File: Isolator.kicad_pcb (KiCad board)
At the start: 2 copper layers, 33 x 67.3 mm, 35 parts, among them J1 Step_0_In, J2 Step_0_Out, J3 Step_1_In, J4 Step_1_Out, J5 UART_In, J6 UART_Out, U1 ISO6741, U2 ISO6741, U3 ISO6721

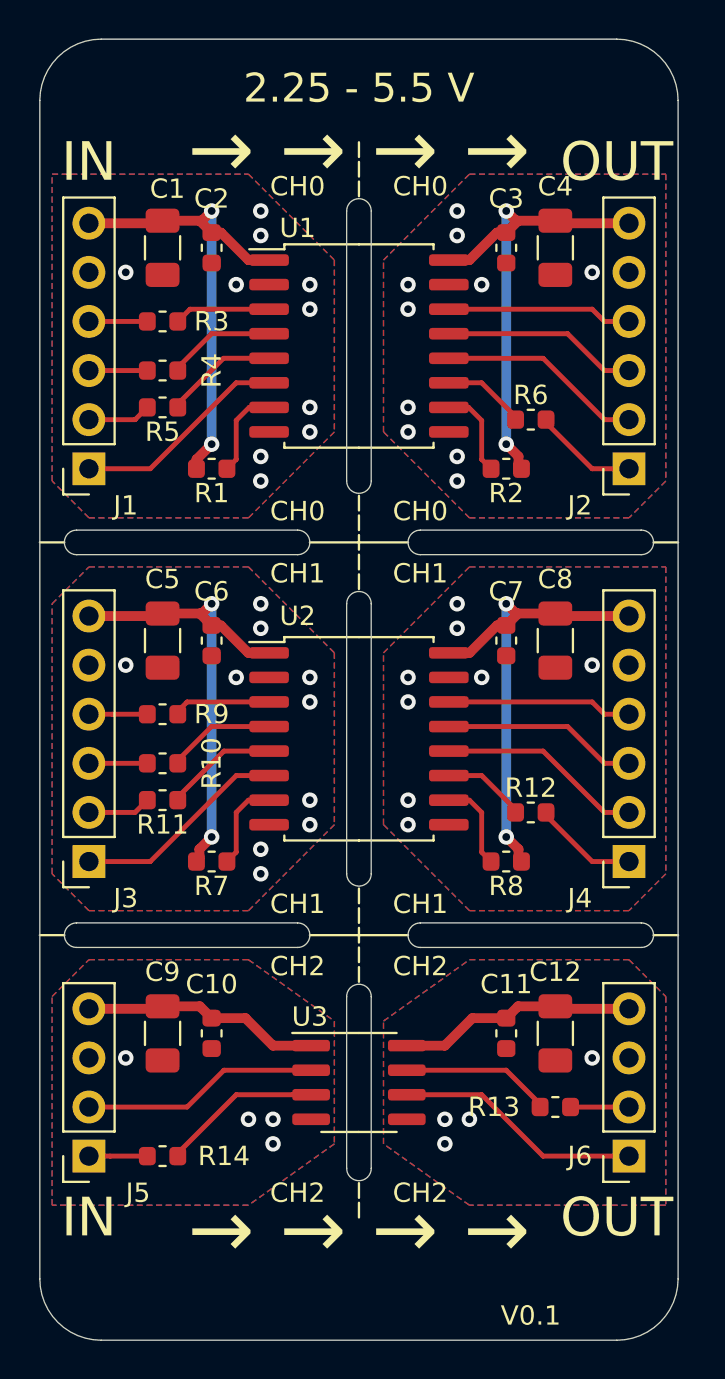
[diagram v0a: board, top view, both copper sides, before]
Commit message: Added mounting holes. (They got lost somehow)
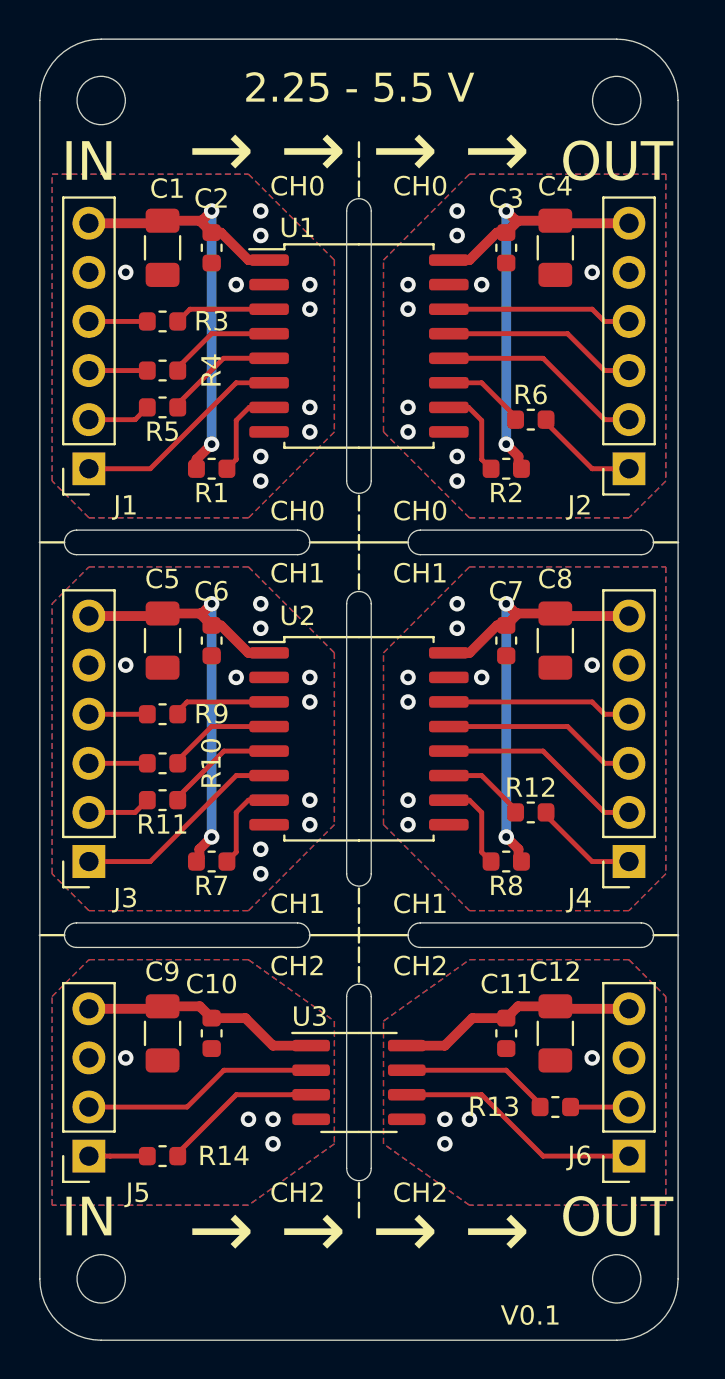
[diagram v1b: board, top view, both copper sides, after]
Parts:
- added  : , MountingHole:MountingHole_2.5mm, F.Cu at (142.9, 55.9)
- added  : , MountingHole:MountingHole_2.5mm, F.Cu at (169.5, 55.9)
- added  : , MountingHole:MountingHole_2.5mm, F.Cu at (169.5, 116.8)
- added  : , MountingHole:MountingHole_2.5mm, F.Cu at (142.9, 116.8)
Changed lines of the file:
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@@
     (tracks 213)
     (zones 0)
-    (modules 35)
+    (modules 39)
     (nets 47)
   )
@@
     (add_net "Net-(R9-Pad2)")
   )
+  (module MountingHole:MountingHole_2.5mm (layer F.Cu)
+    (at 142.875 55.88)
+    (descr "Mounting Hole 2.5mm, no annular")
+    (tags "mounting hole 2.5mm no annular")
+    (attr virtual)
+    (fp_text reference " " (at 0 -3.5) (layer F.SilkS) hide
+      (effects (font (size 1 1) (thickness 0.15)))
+    )
+    (fp_text value " " (at 0 3.5) (layer F.Fab) hide
+      (effects (font (size 1 1) (thickness 0.15)))
+    )
+    (fp_text user " " (at 0.3 0) (layer F.Fab) hide
+      (effects (font (size 1 1) (thickness 0.15)))
+    )
+    (fp_circle (center 0 0) (end 2.5 0) (layer Cmts.User) (width 0.15))
+    (fp_circle (center 0 0) (end 2.75 0) (layer F.CrtYd) (width 0.05))
+    (pad 1 np_thru_hole circle (at 0 0) (size 2.5 2.5) (drill 2.5) (layers *.Cu *.Mask))
+  )
+  (module MountingHole:MountingHole_2.5mm (layer F.Cu)
+    (at 169.545 55.88)
+    (descr "Mounting Hole 2.5mm, no annular")
+    (tags "mounting hole 2.5mm no annular")
+    (attr virtual)
+    (fp_text reference " " (at 0 -3.5) (layer F.SilkS) hide
+      (effects (font (size 1 1) (thickness 0.15)))
+    )
+    (fp_text value " " (at 0 3.5) (layer F.Fab) hide
+      (effects (font (size 1 1) (thickness 0.15)))
+    )
+    (fp_circle (center 0 0) (end 2.75 0) (layer F.CrtYd) (width 0.05))
+    (fp_circle (center 0 0) (end 2.5 0) (layer Cmts.User) (width 0.15))
+    (fp_text user " " (at 0.3 0) (layer F.Fab) hide
+      (effects (font (size 1 1) (thickness 0.15)))
+    )
+    (pad 1 np_thru_hole circle (at 0 0) (size 2.5 2.5) (drill 2.5) (layers *.Cu *.Mask))
+  )
+  (module MountingHole:MountingHole_2.5mm (layer F.Cu)
+    (at 169.545 116.84)
+    (descr "Mounting Hole 2.5mm, no annular")
+    (tags "mounting hole 2.5mm no annular")
+    (attr virtual)
+    (fp_text reference " " (at 0 -3.5) (layer F.SilkS) hide
+      (effects (font (size 1 1) (thickness 0.15)))
+    )
+    (fp_text value " " (at 0 3.5) (layer F.Fab) hide
+      (effects (font (size 1 1) (thickness 0.15)))
+    )
+    (fp_text user " " (at 0.3 0) (layer F.Fab) hide
+      (effects (font (size 1 1) (thickness 0.15)))
+    )
+    (fp_circle (center 0 0) (end 2.5 0) (layer Cmts.User) (width 0.15))
+    (fp_circle (center 0 0) (end 2.75 0) (layer F.CrtYd) (width 0.05))
+    (pad 1 np_thru_hole circle (at 0 0) (size 2.5 2.5) (drill 2.5) (layers *.Cu *.Mask))
+  )
+  (module MountingHole:MountingHole_2.5mm (layer F.Cu)
+    (at 142.875 116.84)
+    (descr "Mounting Hole 2.5mm, no annular")
+    (tags "mounting hole 2.5mm no annular")
+    (attr virtual)
+    (fp_text reference " " (at 0 -3.5) (layer F.SilkS) hide
+      (effects (font (size 1 1) (thickness 0.15)))
+    )
+    (fp_text value " " (at 0 3.5) (layer F.Fab) hide
+      (effects (font (size 1 1) (thickness 0.15)))
+    )
+    (fp_circle (center 0 0) (end 2.75 0) (layer F.CrtYd) (width 0.05))
+    (fp_circle (center 0 0) (end 2.5 0) (layer Cmts.User) (width 0.15))
+    (fp_text user " " (at 0.3 0) (layer F.Fab) hide
+      (effects (font (size 1 1) (thickness 0.15)))
+    )
+    (pad 1 np_thru_hole circle (at 0 0) (size 2.5 2.5) (drill 2.5) (layers *.Cu *.Mask))
+  )
   (module Resistor_SMD:R_0603_1608Metric (layer F.Cu)

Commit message: Added fiducials to single board
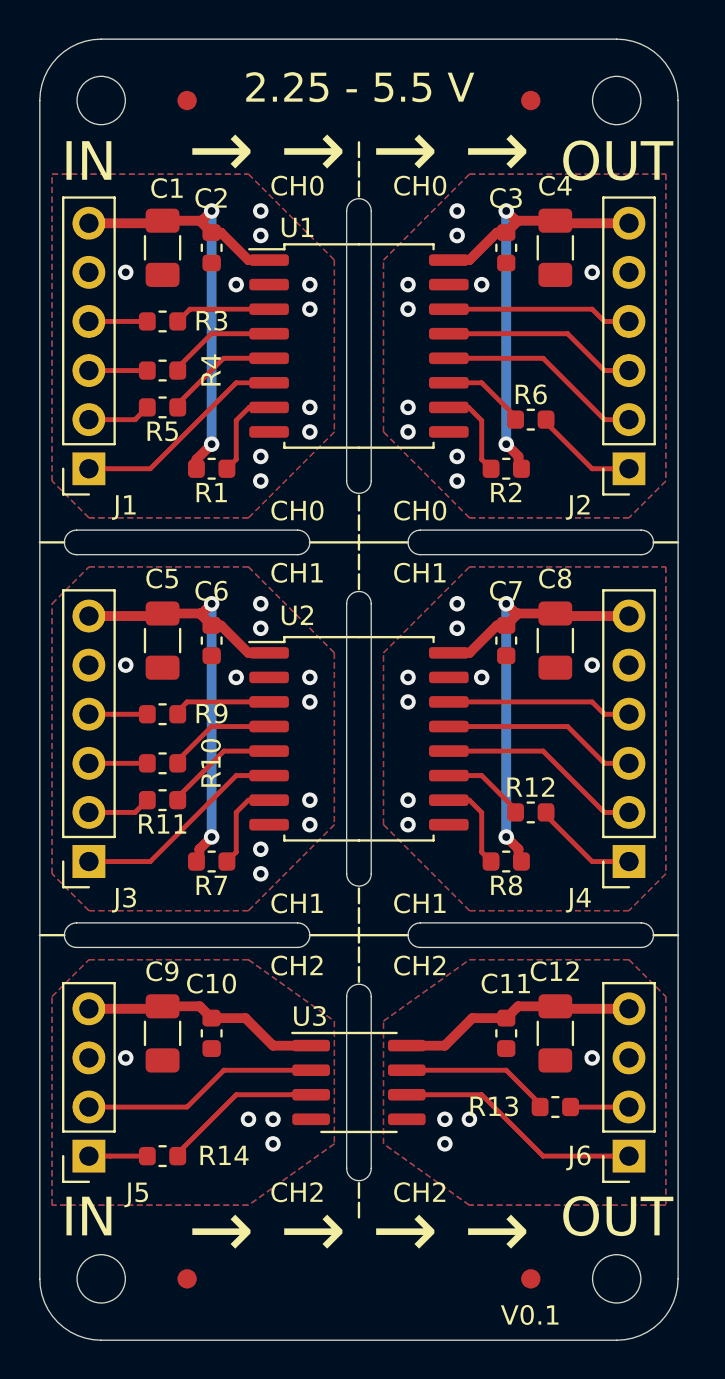
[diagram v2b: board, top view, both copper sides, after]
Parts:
- added  : , Fiducial:Fiducial_1mm_Dia_2mm_Outer, F.Cu at (147.3, 55.9)
- added  : , Fiducial:Fiducial_1mm_Dia_2mm_Outer, F.Cu at (165.1, 55.9)
- added  : , Fiducial:Fiducial_1mm_Dia_2mm_Outer, F.Cu at (165.1, 116.8)
- added  : , Fiducial:Fiducial_1mm_Dia_2mm_Outer, F.Cu at (147.3, 116.8)
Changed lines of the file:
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@@
     (tracks 213)
     (zones 0)
-    (modules 39)
+    (modules 43)
     (nets 47)
   )
@@
   )
   (setup
-    (last_trace_width 0.25)
+    (last_trace_width 0.127)
     (user_trace_width 0.127)
     (user_trace_width 0.254)
@@
     (add_net "Net-(R9-Pad2)")
   )
+  (module Fiducial:Fiducial_1mm_Dia_2mm_Outer (layer F.Cu)
+    (at 147.32 55.88)
+    (descr "Circular Fiducial, 1mm bare copper top, 2mm keepout (Level A)")
+    (tags fiducial)
+    (attr smd)
+    (fp_text reference " " (at 0 -2) (layer F.SilkS) hide
+      (effects (font (size 1 1) (thickness 0.15)))
+    )
+    (fp_text value " " (at 0 2) (layer F.Fab) hide
+      (effects (font (size 1 1) (thickness 0.15)))
+    )
+    (fp_circle (center 0 0) (end 1 0) (layer F.Fab) (width 0.1))
+    (fp_text user " " (at 0 0) (layer F.Fab) hide
+      (effects (font (size 0.4 0.4) (thickness 0.06)))
+    )
+    (fp_circle (center 0 0) (end 1.25 0) (layer F.CrtYd) (width 0.05))
+    (pad "" smd circle (at 0 0) (size 1 1) (layers F.Cu F.Mask)
+      (solder_mask_margin 0.5) (clearance 0.5))
+  )
+  (module Fiducial:Fiducial_1mm_Dia_2mm_Outer (layer F.Cu)
+    (at 165.1 55.88)
+    (descr "Circular Fiducial, 1mm bare copper top, 2mm keepout (Level A)")
+    (tags fiducial)
+    (attr smd)
+    (fp_text reference " " (at 0 -2) (layer F.SilkS) hide
+      (effects (font (size 1 1) (thickness 0.15)))
+    )
+    (fp_text value " " (at 0 2) (layer F.Fab) hide
+      (effects (font (size 1 1) (thickness 0.15)))
+    )
+    (fp_circle (center 0 0) (end 1.25 0) (layer F.CrtYd) (width 0.05))
+    (fp_text user " " (at 0 0) (layer F.Fab) hide
+      (effects (font (size 0.4 0.4) (thickness 0.06)))
+    )
+    (fp_circle (center 0 0) (end 1 0) (layer F.Fab) (width 0.1))
+    (pad "" smd circle (at 0 0) (size 1 1) (layers F.Cu F.Mask)
+      (solder_mask_margin 0.5) (clearance 0.5))
+  )
+  (module Fiducial:Fiducial_1mm_Dia_2mm_Outer (layer F.Cu)
+    (at 165.1 116.84)
+    (descr "Circular Fiducial, 1mm bare copper top, 2mm keepout (Level A)")
+    (tags fiducial)
+    (attr smd)
+    (fp_text reference " " (at 0 -2) (layer F.SilkS) hide
+      (effects (font (size 1 1) (thickness 0.15)))
+    )
+    (fp_text value " " (at 0 2) (layer F.Fab) hide
+      (effects (font (size 1 1) (thickness 0.15)))
+    )
+    (fp_circle (center 0 0) (end 1 0) (layer F.Fab) (width 0.1))
+    (fp_text user " " (at 0 0) (layer F.Fab) hide
+      (effects (font (size 0.4 0.4) (thickness 0.06)))
+    )
+    (fp_circle (center 0 0) (end 1.25 0) (layer F.CrtYd) (width 0.05))
+    (pad "" smd circle (at 0 0) (size 1 1) (layers F.Cu F.Mask)
+      (solder_mask_margin 0.5) (clearance 0.5))
+  )
+  (module Fiducial:Fiducial_1mm_Dia_2mm_Outer (layer F.Cu)
+    (at 147.32 116.84)
+    (descr "Circular Fiducial, 1mm bare copper top, 2mm keepout (Level A)")
+    (tags fiducial)
+    (attr smd)
+    (fp_text reference " " (at 0 -2) (layer F.SilkS) hide
+      (effects (font (size 1 1) (thickness 0.15)))
+    )
+    (fp_text value " " (at 0 2) (layer F.Fab) hide
+      (effects (font (size 1 1) (thickness 0.15)))
+    )
+    (fp_circle (center 0 0) (end 1.25 0) (layer F.CrtYd) (width 0.05))
+    (fp_text user " " (at 0 0) (layer F.Fab) hide
+      (effects (font (size 0.4 0.4) (thickness 0.06)))
+    )
+    (fp_circle (center 0 0) (end 1 0) (layer F.Fab) (width 0.1))
+    (pad "" smd circle (at 0 0) (size 1 1) (layers F.Cu F.Mask)
+      (solder_mask_margin 0.5) (clearance 0.5))
+  )
   (module MountingHole:MountingHole_2.5mm (layer F.Cu)
